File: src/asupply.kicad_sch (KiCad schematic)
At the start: 124 parts, among them U10 LT3081xDF, U11 LT3042xMSE, U12 LT3045xMSE, U13 LT3045xMSE, U14 LT3042xMSE, U15 LT3094xMSE, U16 LTC3261, U17 LT3042xMSE

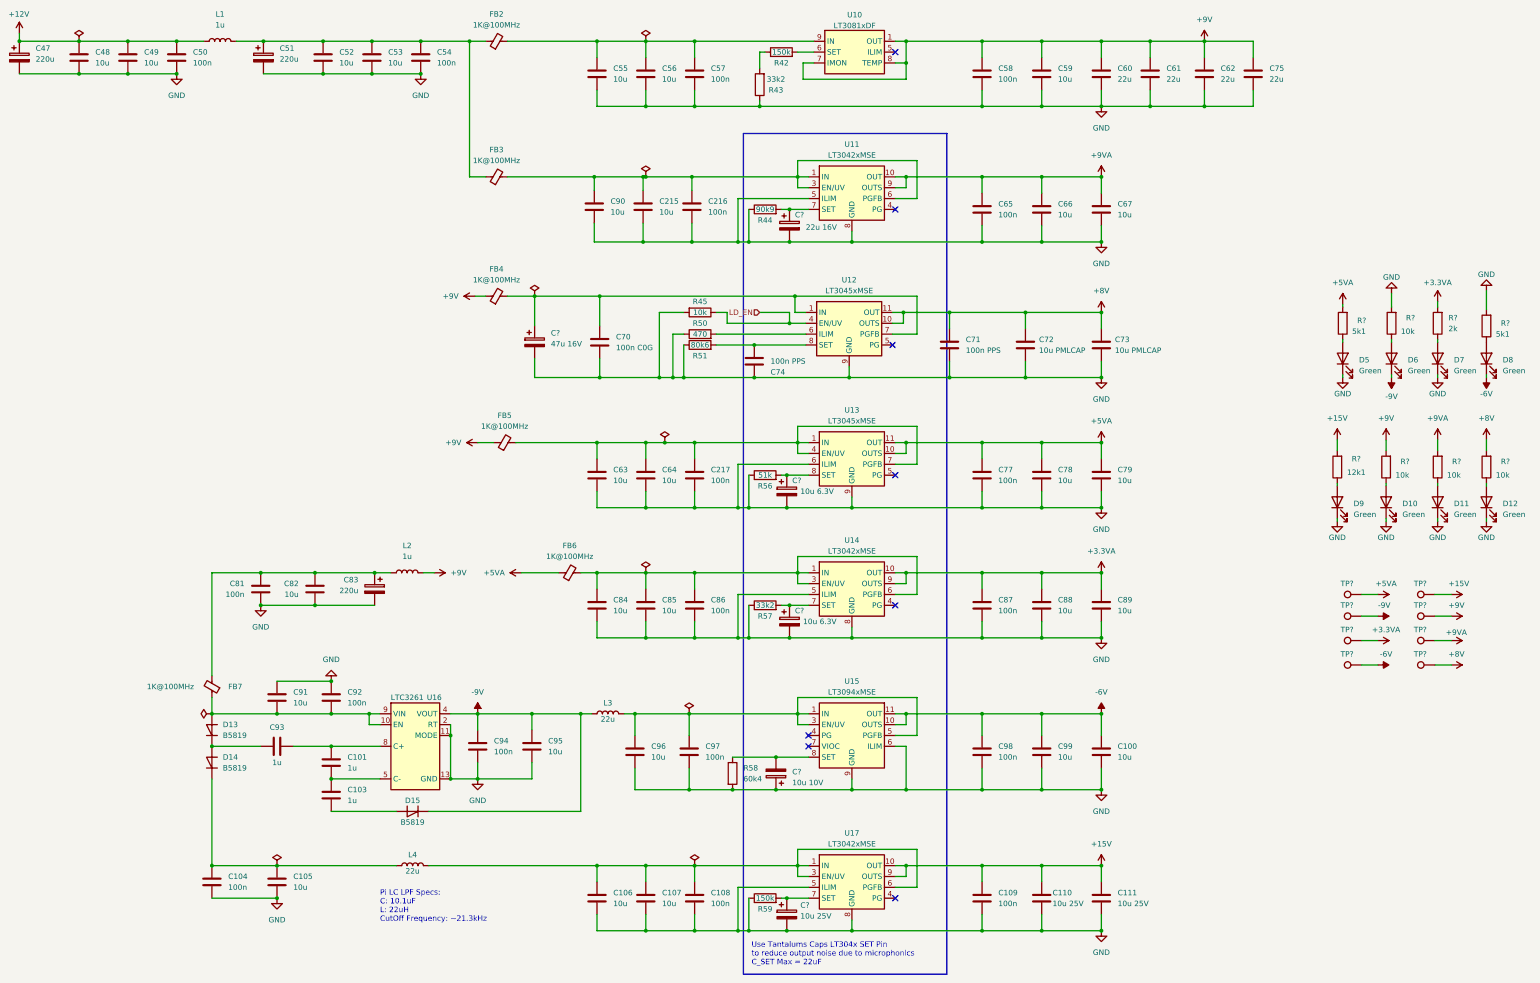
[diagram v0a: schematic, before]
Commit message: Fix issiues from lis, see bug/issiue list in DOC directory
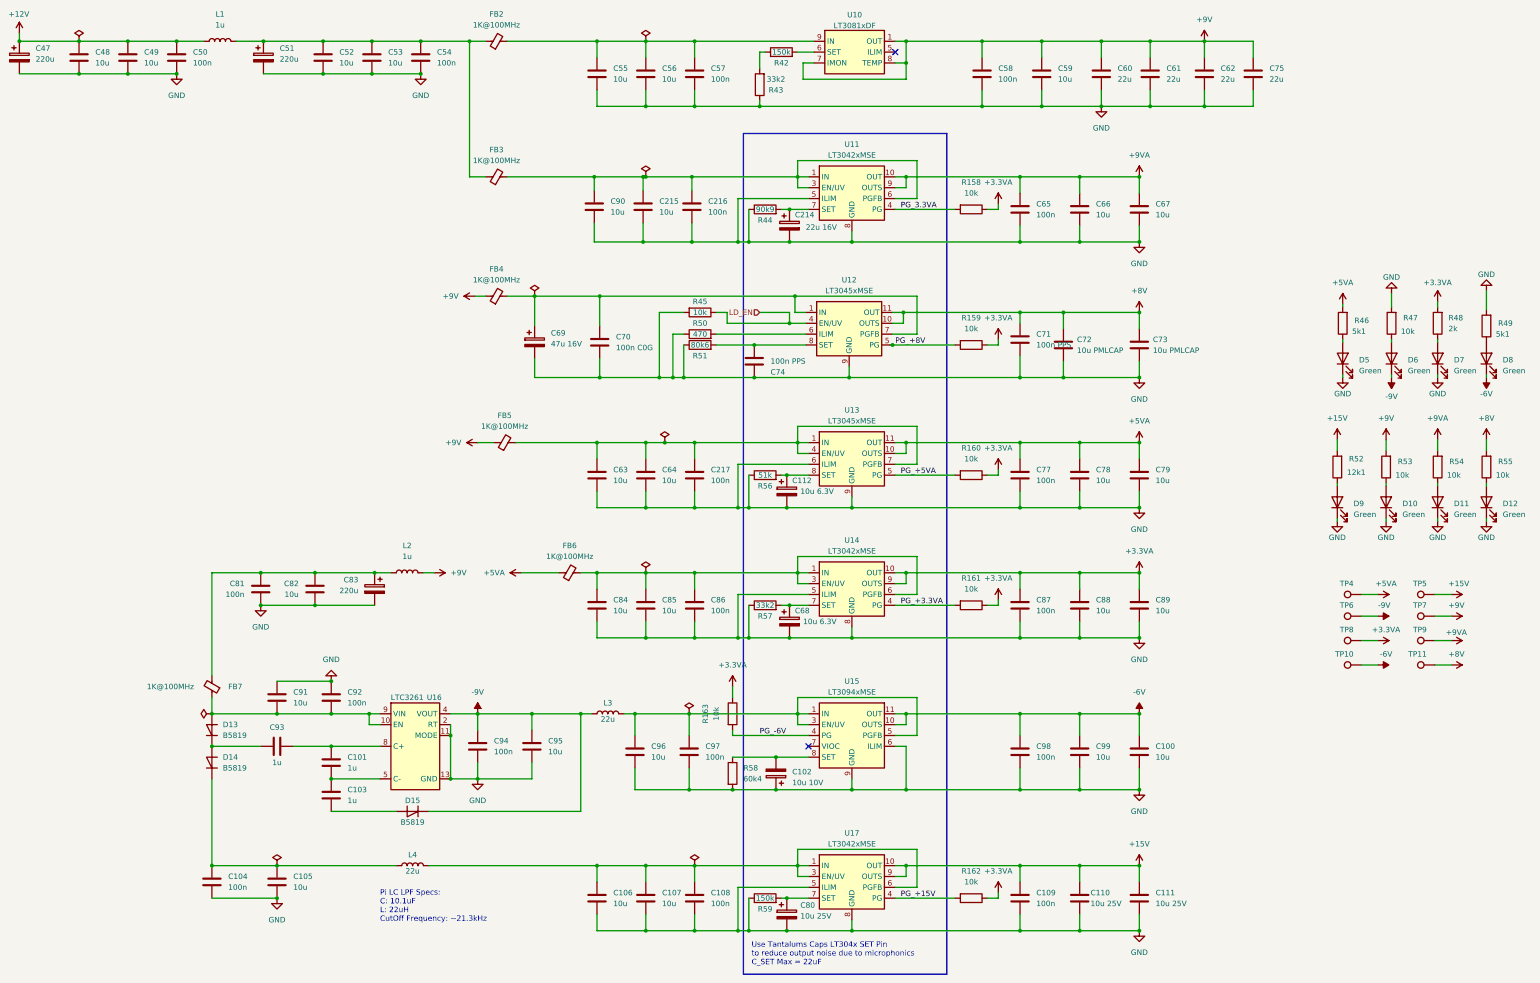
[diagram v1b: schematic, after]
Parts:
- added R158, R159, R160, R161, R162, R163: 10k, Resistor_SMD:R_0603_1608Metric, symbol Device:R
- gave numbers to parts that had none: 22
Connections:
- net +3.3VA: now also R158.1, R159.1, R160.1, R161.1, R162.1, R163.1
- net PG_3.3VA: now reaches U11.4 (PG)
- net PG_3.3VA: now also R158.2
- net PG_+3.3VA: now reaches U14.4 (PG)
- net PG_+3.3VA: now also R161.2
- net PG_+8V: now reaches U12.5 (PG)
- net PG_+8V: now also R159.2
- net PG_+15V: now reaches U17.4 (PG)
- net PG_+15V: now also R162.2
- net PG_-6V: now reaches U15.4 (PG)
- net PG_-6V: now also R163.2
- net PG_+5VA: now reaches U13.5 (PG)
- net PG_+5VA: now also R160.2
- no-connect marks 8 -> 2
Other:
- moved on the sheet: C100, C109, C110, C111, C65, C66, C67, C71, C72, C73, C77, C78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
